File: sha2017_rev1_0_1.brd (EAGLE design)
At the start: 95 x 86 mm, 201 parts, among them IC1 CP210X_USB_UART, IC2 LD117AS33TR, IC3 ESP32WROOM32, IC4 TP4056, M1 MOTOR10MM, Q1 MMBT2222A, Q2 MMBT2222A, Q3 MMBT2222A, Q4 MMBT2222A, Q5 SI1304 BDL, Q6 MMBT2222A, U1 MPR121QR2, X2 2908-05WB-MG, X4 JST-PH3

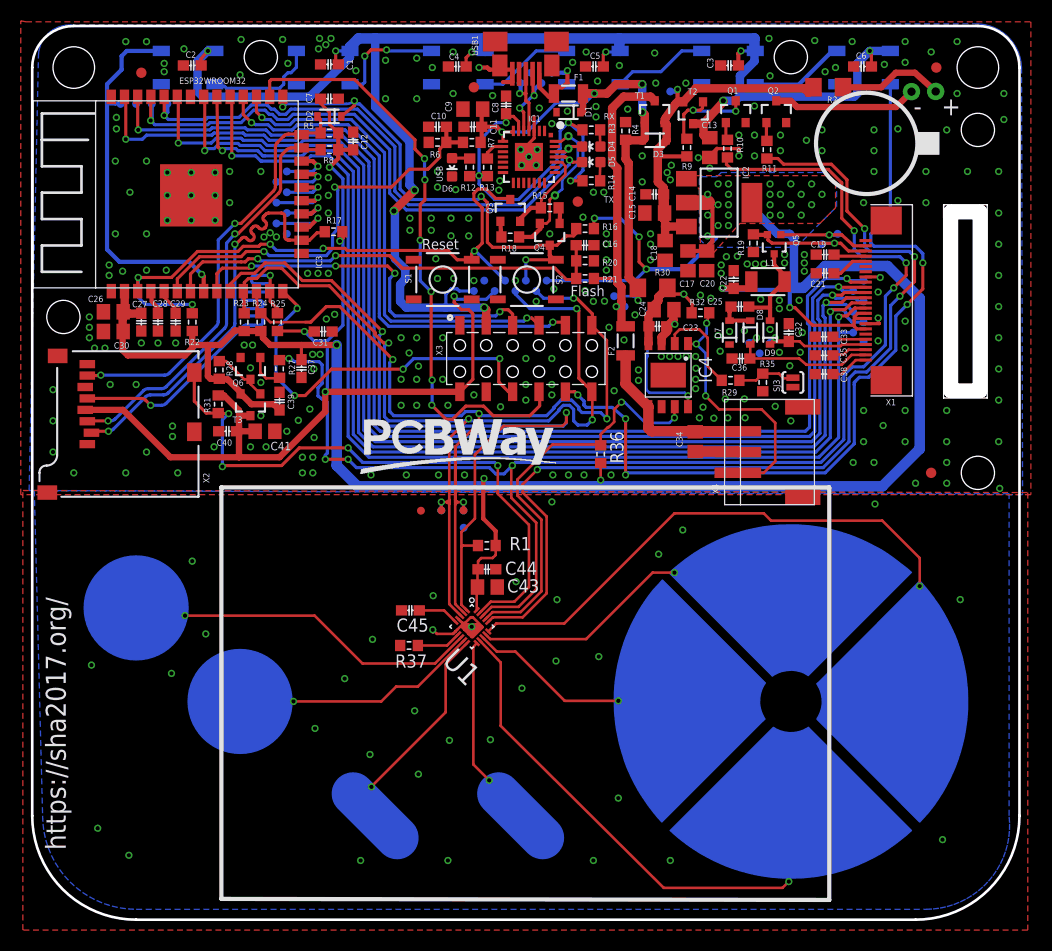
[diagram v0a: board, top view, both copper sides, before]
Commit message: Fixed DRU Fixed routing adjust lables and increase size
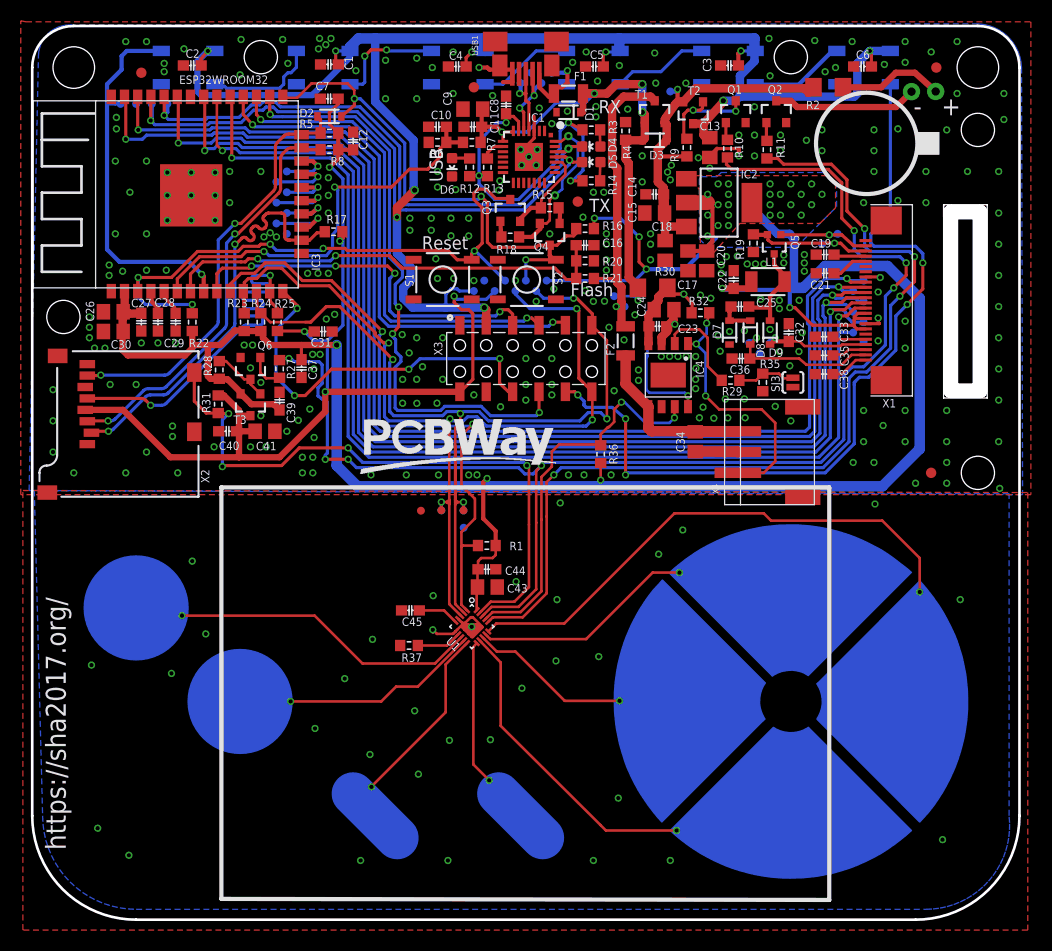
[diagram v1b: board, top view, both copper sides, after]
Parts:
- moved $$U$9 0.81 mm to (50.8, 39.1)
- turned C7 to 180 degrees
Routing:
- net I2C_INT: track 75.4 -> 58.3 mm
- net VIBRATOR: track 93.2 -> 90.1 mm
- net I2C_SDA: track 94.3 -> 91.8 mm
- net N$44: track 44.3 -> 42.0 mm
- net CHRG_STAT: track 39.9 -> 37.6 mm
- net SD_CD: track 58.6 -> 60.2 mm
- net ESP32_FLASH: track 50.7 -> 52.2 mm, vias 4 -> 3
- net I2C_SCL: track 92.9 -> 91.6 mm
- net WS2812_POWER_EN: track 130.4 -> 129.7 mm
- net LCD_CS: track 113.2 -> 112.6 mm
- net WS2812_POWER: track 153.8 -> 153.3 mm
- net EXTIO-3: track 58.2 -> 57.9 mm, vias 6 -> 4

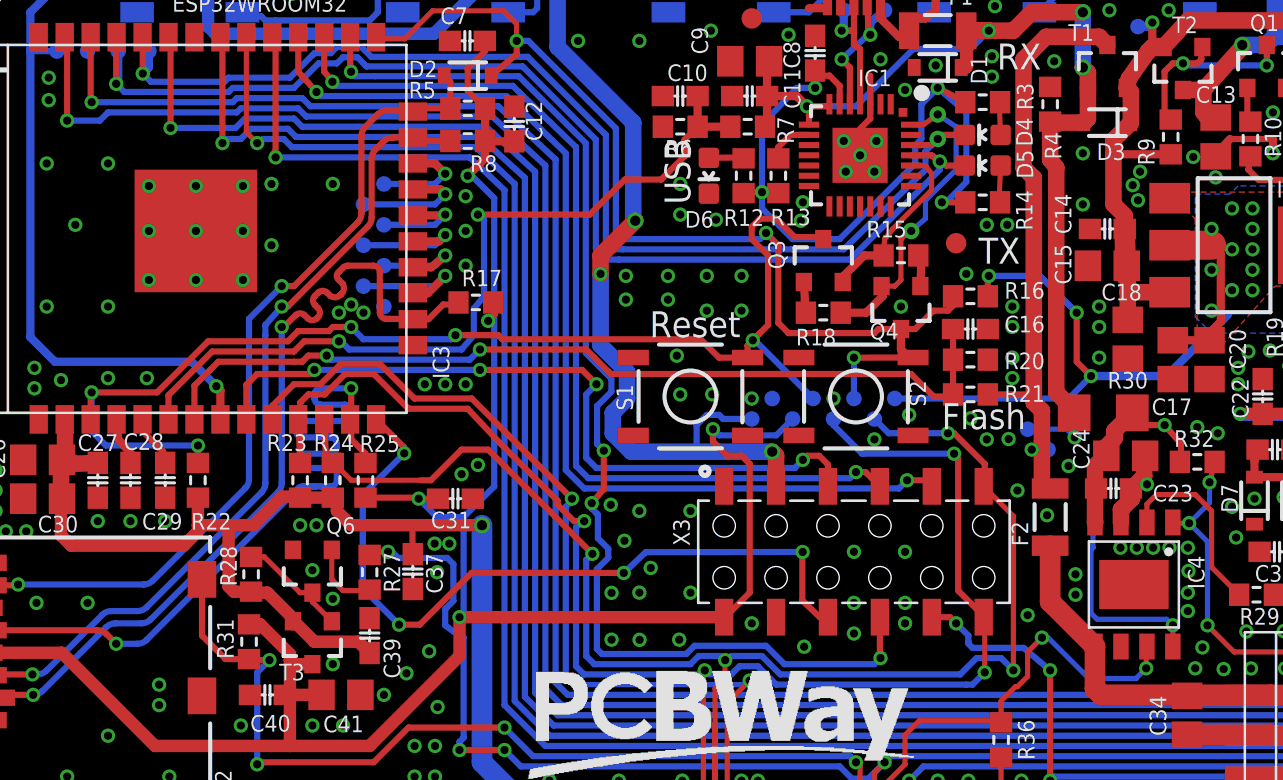
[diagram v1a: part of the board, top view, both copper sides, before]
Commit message: rerout extio-4 and added register holes ext socket
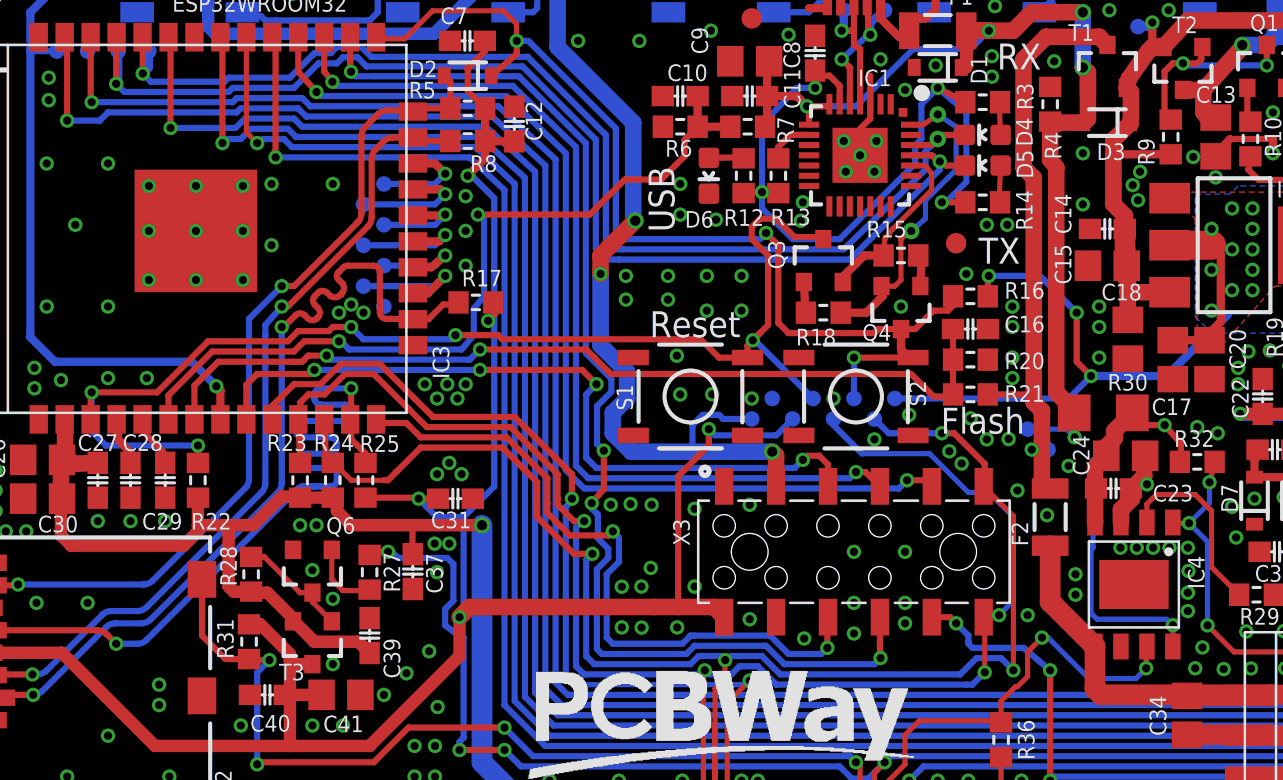
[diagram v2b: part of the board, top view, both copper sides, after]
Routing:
- net EXTIO-4: track 37.4 -> 33.7 mm, vias 4 -> 2
- net I2C_SDA: track 91.8 -> 94.1 mm
- net I2C_SCL: track 91.6 -> 92.7 mm
- net 3V3_SWITCHED: track 107.9 -> 107.0 mm
- net I2C_INT: track 58.3 -> 59.0 mm
- net GND: vias 300 -> 306
